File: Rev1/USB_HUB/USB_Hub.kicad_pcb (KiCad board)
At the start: 4 copper layers, 95.9 x 90.2 mm, 79 parts, among them IC1 TLV76733DGNR, IC2 TLV76733DGNR, IC3 USB2513B_M2, IC4 USB2513B_M2, J1 826629-4, J2 826629-4, J4 F3311A7H121014E200, J6 B4B-XH-A, J9 B4B-XH-A, Q1 IRLML2244TRPBF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

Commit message: USB HUB Finalized
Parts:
- moved JP6 49.7 mm to (113.5, 139.0)
- moved Q7 49.7 mm to (113.5, 135.9)
- moved R13 49.7 mm to (110.7, 135.9)
- moved Q3 40.2 mm to (169.2, 55.9), turned to -90 degrees
- moved R24 39.9 mm to (171.8, 56.2), turned to 90 degrees
- moved JP8 36.3 mm to (166.1, 55.8), turned to 90 degrees
- moved JP10 29.0 mm to (193.3, 69.7)
- moved Q5 29.0 mm to (193.4, 66.7)
- moved R25 29.0 mm to (190.6, 66.7)
- moved J4 7.87 mm to (106.4, 67.2)
- moved R26 5.27 mm to (191.0, 74.2)
- moved JP9 5.27 mm to (193.7, 77.2)
- moved Q4 5.22 mm to (194.0, 74.2)
- moved USB_C4 3.03 mm to (158.5, 96.0)
- moved USB_C1 3.01 mm to (149.0, 102.6)
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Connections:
- net Net-(D1-input/output_1_1) renamed /Upstream/P2+
- net Net-(D1-input/output_2_1) renamed /Upstream/P2-
- net Net-(IC3-USBDM_UP) renamed /hub_1/1-
- net Net-(IC3-USBDP_UP) renamed /hub_1/1+
- net Net-(IC4-USBDM_UP) renamed /hub_2/2-
- net Net-(IC4-USBDP_UP) renamed /hub_2/2+
- D3 pad 1: Net-(D3-input/output_1_1) -> /Upstream/P1-
- D3 pad 3: Net-(D3-input/output_2_1) -> /Upstream/P1+
- D3 pad 4: D_N_1 -> D_1_P
- D3 pad 6: D_P_1 -> D_1_N
- J4 pad 10: Net-(D3-input/output_2_1) -> /Upstream/P1-
- J4 pad 11: Net-(D3-input/output_1_1) -> /Upstream/P1+
- R10 pad 1: D_P_1 -> D_1_P
- R9 pad 1: D_N_1 -> D_1_N
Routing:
- net /Upstream/P1-: track 0.00 -> 113.6 mm, vias 0 -> 2
- net /Upstream/P1+: track 0.00 -> 111.0 mm, vias 0 -> 2
- net Net-(D3-input/output_2_1): track 93.0 -> 0.00 mm, vias 2 -> 0
- net Net-(D3-input/output_1_1): track 78.8 -> 0.00 mm, vias 2 -> 0
- net Net-(JP6-A): track 13.3 -> 76.4 mm, vias 0 -> 2
- net PRTPWR1: track 57.1 -> 17.0 mm, vias 2 -> 0
- net Net-(JP8-A): track 14.2 -> 52.7 mm, vias 1 -> 2
- net Net-(JP10-A): track 9.29 -> 37.0 mm
- net PORT2_P: track 38.6 -> 65.9 mm, vias 2 -> 0
- net PORT2_N: track 40.3 -> 66.7 mm, vias 2 -> 0
- net /Upstream/P2+: track 84.9 -> 110.3 mm
- net /Upstream/P2-: track 89.0 -> 109.1 mm
- net PRTPWR4: track 47.0 -> 27.4 mm
- net PRTPWR6: track 26.2 -> 12.7 mm
- net PRTPWR3: track 35.8 -> 22.6 mm
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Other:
- outline, holes or cut-outs redrawn

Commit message: Updated USB HUB
Based on Mechanical Feedback
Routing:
- net PORT2_P: track 65.9 -> 81.4 mm
- net PORT2_N: track 66.7 -> 82.2 mm
- net Net-(JP5-A): track 57.9 -> 63.2 mm
- net /Upstream/P1-: track 113.6 -> 118.8 mm
- net /Upstream/P1+: track 111.0 -> 116.2 mm
- net Net-(JP8-A): track 52.7 -> 55.0 mm
- net /Upstream/P2-: track 109.1 -> 111.4 mm
- net /Upstream/P2+: track 110.3 -> 112.6 mm
- net Net-(JP6-A): track 76.4 -> 78.7 mm
- net Net-(JP9-A): track 61.1 -> 62.8 mm
- net GND: track 124.9 -> 125.7 mm, vias 56 -> 55
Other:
- outline, holes or cut-outs redrawn

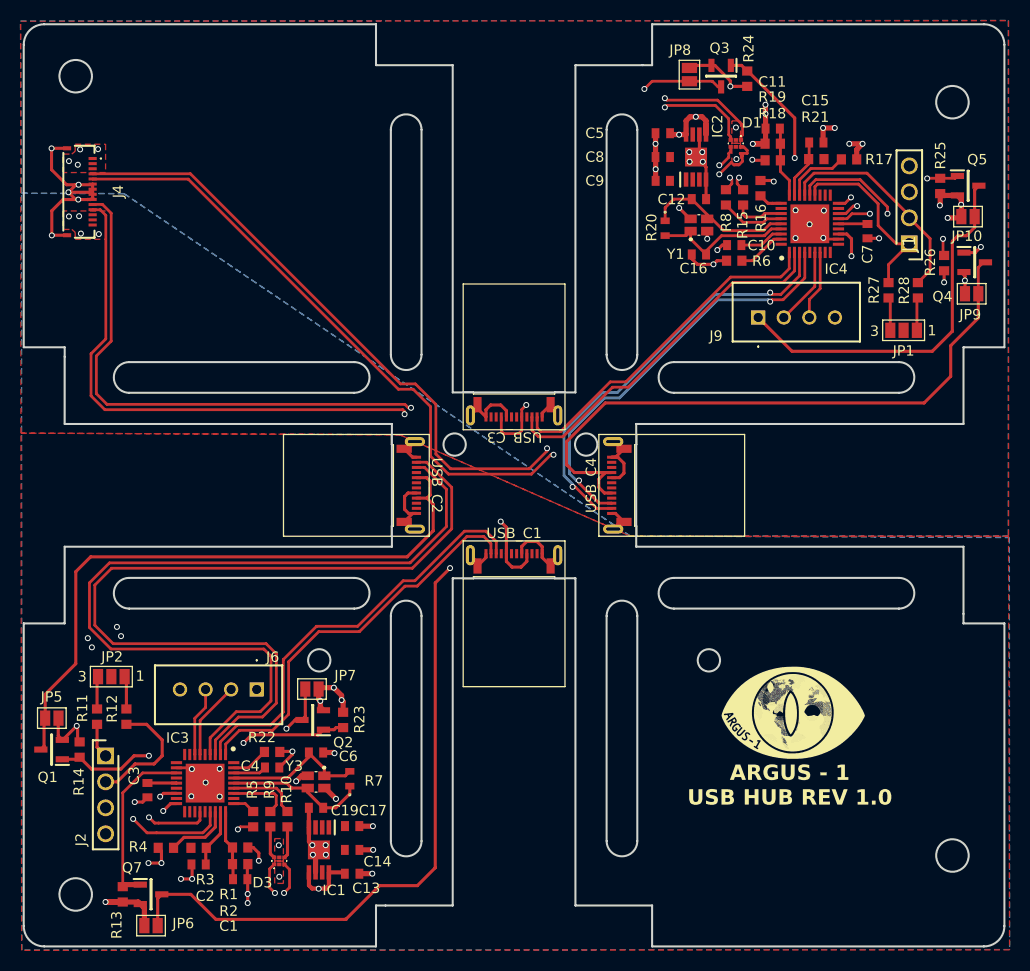
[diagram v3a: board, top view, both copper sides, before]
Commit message: USB HUB Updated
Based on TA feedback
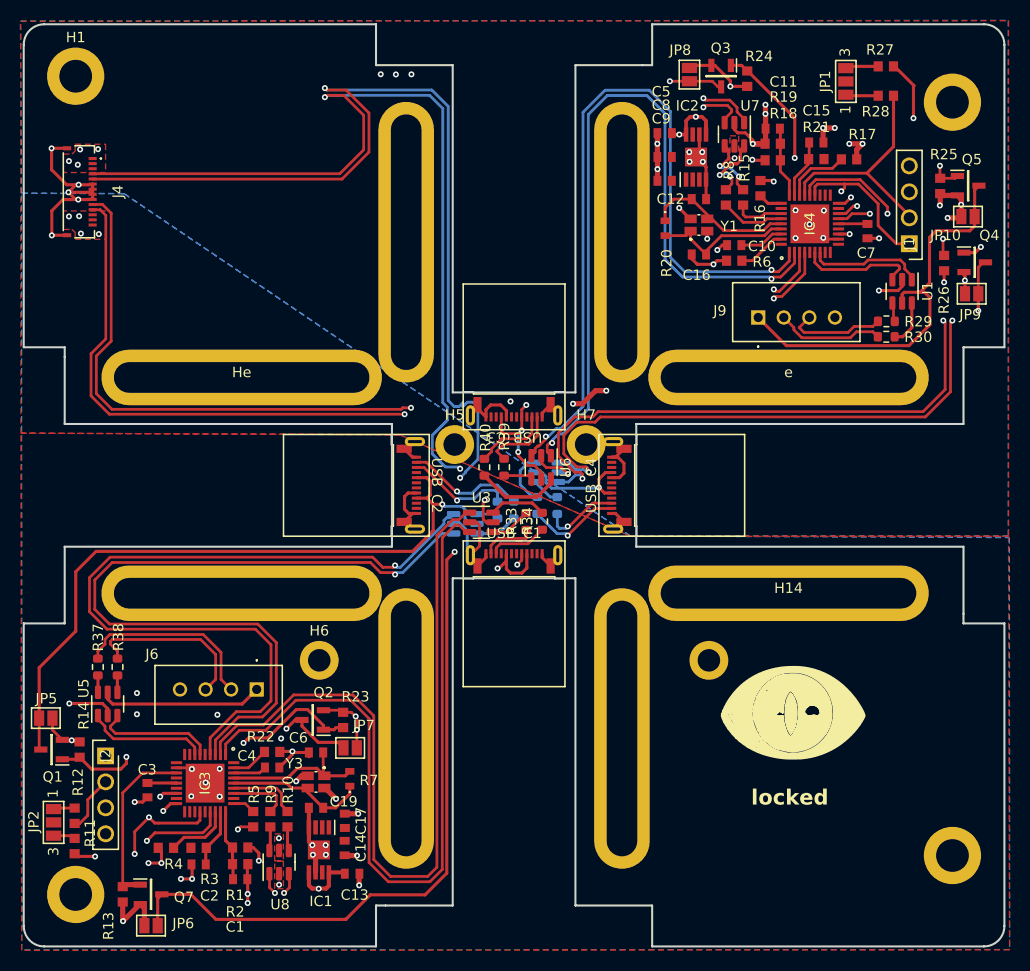
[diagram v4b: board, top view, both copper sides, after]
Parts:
- removed D1, D3: PRTR5V0U2F,115, SamacSys_Parts:PESD3V3L5UF115
- added H1: MountingHole_Pad, MountingHole:MountingHole_3.2mm_M3_DIN965_Pad, F.Cu at (106.1, 56.0)
- added H10: MountingHole_Pad, MountingHole:MountingHole_USB, F.Cu at (159.5, 119.7)
- added H11: MountingHole_Pad, MountingHole:MountingHole_USB, F.Cu at (138.4, 119.7)
- added H13: MountingHole_Pad, MountingHole:MountingHole_USB, F.Cu at (138.4, 72.2)
- added H14: MountingHole_Pad, MountingHole:MountingHole_USB, F.Cu at (175.8, 106.5)
- added H16: MountingHole_Pad, MountingHole:MountingHole_USB, F.Cu at (122.3, 106.5)
- added H2: MountingHole_Pad, MountingHole:MountingHole_3.2mm_M3_DIN965_Pad, F.Cu at (191.8, 58.5)
- added H3: MountingHole_Pad, MountingHole:MountingHole_3.2mm_M3_DIN965_Pad, F.Cu at (191.8, 132.2)
- added H4: MountingHole_Pad, MountingHole:MountingHole_3.2mm_M3_DIN965_Pad, F.Cu at (106.1, 136.0)
- added H5: MountingHole_Pad, MountingHole:MountingHole_2.2mm_M2_DIN965_Pad, F.Cu at (143.1, 92.0)
- added H6: MountingHole_Pad, MountingHole:MountingHole_2.2mm_M2_DIN965_Pad, F.Cu at (129.9, 113.1)
- added H7: MountingHole_Pad, MountingHole:MountingHole_2.2mm_M2_DIN965_Pad, F.Cu at (156.0, 92.0)
- added H8: MountingHole_Pad, MountingHole:MountingHole_2.2mm_M2_DIN965_Pad, F.Cu at (168.0, 113.1)
- added H9: MountingHole_Pad, MountingHole:MountingHole_USB, F.Cu at (159.5, 72.2)
- added He: MountingHole_Pad, MountingHole:MountingHole_USB, F.Cu at (122.3, 85.4)
- added R29: 22R, Resistor_SMD:R_0603_1608Metric, F.Cu at (185.4, 79.9)
- added R30: 22R, Resistor_SMD:R_0603_1608Metric, F.Cu at (185.3, 81.4)
- added R31: 22R, Resistor_SMD:R_0603_1608Metric, B.Cu at (151.2, 97.9)
- added R32: 22R, Resistor_SMD:R_0603_1608Metric, B.Cu at (153.2, 97.9)
- added R33: 22R, Resistor_SMD:R_0603_1608Metric, F.Cu at (150.1, 99.5)
- added R34: 22R, Resistor_SMD:R_0603_1608Metric, F.Cu at (151.7, 99.5)
- added R35: 22R, Resistor_SMD:R_0603_1608Metric, B.Cu at (148.9, 98.4)
- added R36: 22R, Resistor_SMD:R_0603_1608Metric, B.Cu at (147.3, 98.4)
- added R37: 22R, Resistor_SMD:R_0603_1608Metric, F.Cu at (108.3, 113.7)
- added R38: 22R, Resistor_SMD:R_0603_1608Metric, F.Cu at (110.2, 113.7)
- added R39: 22R, Resistor_SMD:R_0603_1608Metric, F.Cu at (148.0, 94.2)
- added R40: 22R, Resistor_SMD:R_0603_1608Metric, F.Cu at (146.1, 94.2)
- added U1: USBLC6-2SC6, Package_TO_SOT_SMD:SOT-23-6, F.Cu at (186.9, 77.0)
- added U2: USBLC6-2SC6, Package_TO_SOT_SMD:SOT-23-6, B.Cu at (152.2, 94.7)
- added U3: USBLC6-2SC6, Package_TO_SOT_SMD:SOT-23-6, F.Cu at (145.8, 99.6)
- added U4: USBLC6-2SC6, Package_TO_SOT_SMD:SOT-23-6, B.Cu at (144.2, 99.7)
- added U5: USBLC6-2SC6, Package_TO_SOT_SMD:SOT-23-6, F.Cu at (109.2, 117.3)
- added U6: USBLC6-2SC6, Package_TO_SOT_SMD:SOT-23-6, F.Cu at (151.6, 94.2)
- added U7: USBLC6-2SC6, Package_TO_SOT_SMD:SOT-23-6, F.Cu at (170.5, 61.6)
- added U8: USBLC6-2SC6, Package_TO_SOT_SMD:SOT-23-6, F.Cu at (126.0, 132.8)
- added e: MountingHole_Pad, MountingHole:MountingHole_USB, F.Cu at (175.8, 85.4)
- moved JP1 25.0 mm to (181.4, 56.5), turned to 90 degrees
- moved R27 21.9 mm to (185.3, 55.0), turned to 180 degrees
- moved R28 19.3 mm to (185.3, 57.9), turned to 180 degrees
- moved JP2 15.3 mm to (103.9, 128.9), turned to -90 degrees
- moved R11 12.8 mm to (106.0, 131.2)
- moved R12 10.9 mm to (106.0, 128.3)
- moved JP7 6.86 mm to (132.9, 121.6)
- moved C17 0.88 mm to (132.4, 128.8), turned to -90 degrees
- moved C14 0.76 mm to (132.4, 131.4), turned to 90 degrees
- moved JP5 0.59 mm to (103.2, 118.7)
- moved C8 0.18 mm to (163.7, 63.9)
- moved C5 0.18 mm to (163.7, 61.5)
- moved C9 0.18 mm to (163.7, 66.2)
- turned C6 to 0 degrees
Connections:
- J6 pad 2: PORT3_N -> /Connectors/3-
- J6 pad 3: PORT3_P -> /Connectors/3+
- J9 pad 2: PORT6_N -> /Connectors/6-
- J9 pad 3: PORT6_P -> /Connectors/6+
- USB_C1 pad A06: PORT1_P -> /Connectors/1+
- USB_C1 pad A07: PORT1_N -> /Connectors/1-
- USB_C2 pad A06: PORT2_P -> /Connectors/2+
- USB_C2 pad A07: PORT2_N -> /Connectors/2-
- USB_C3 pad A06: PORT4_P -> /Connectors/4+
- USB_C3 pad A07: PORT4_N -> /Connectors/4-
- USB_C4 pad A06: PORT5_P -> /Connectors/5+
- USB_C4 pad A07: PORT5_N -> /Connectors/5-
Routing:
- net 5V2: track 26.1 -> 72.5 mm, vias 14 -> 20
- net /Upstream/P2-: track 111.4 -> 152.9 mm, vias 2 -> 3
- net PORT4_N: track 34.1 -> 74.3 mm, vias 0 -> 2
- net PORT4_P: track 35.8 -> 74.0 mm, vias 0 -> 2
- net PORT5_P: track 41.4 -> 78.9 mm, vias 2 -> 3
- net PORT5_N: track 42.3 -> 79.1 mm, vias 2 -> 3
- net /Upstream/P2+: track 112.6 -> 149.1 mm, vias 2 -> 3
- net PORT1_N: track 39.7 -> 76.0 mm
- net PORT1_P: track 41.4 -> 76.9 mm
- net GND: track 125.7 -> 148.4 mm, vias 55 -> 57
- net /Connectors/3-: track 0.00 -> 18.5 mm
- net Net-(JP7-A): track 10.1 -> 28.5 mm
- net /Connectors/3+: track 0.00 -> 16.8 mm
- net /hub_2/SDA: track 18.5 -> 31.0 mm, vias 0 -> 2
- net /Connectors/2-: track 0.00 -> 11.8 mm, vias 0 -> 1
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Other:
- outline, holes or cut-outs redrawn
- board text added: "locked"
- board text removed: "ARGUS - 1 USB HUB REV 1.0"
